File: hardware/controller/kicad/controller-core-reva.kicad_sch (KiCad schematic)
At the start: 198 parts, among them J101 12V_ISOLATED_INPUT / JST XH, J102 STM_SWD / 1x6 2.54mm, J103 ESP_UART / 1x6 2.54mm, J104 UI_LINK / WR-MM 16, J105 JP13 NTC / 2 vías, J106 JP5 FLOW ADAPTER / VCC-GND-OC, J107 JP14 DOOR / contacto seco, J108 JP16 VISUAL V1..V8 / XH-8, J109 JP22 WATER / RED-WHITE-BLACK, J110 USB-C SERVICE / USB 2.0, J111 USB BENCH POWER / OPEN, J112 24V_ACTUATOR_INPUT / JST XH, J113 JP3 VALVE / A2506, J114 POWER MONITOR / MEASURE ONLY, J115 JP8 GRINDER / 320VDC, J116 JP19 HEATER / 1900W 27R5, J117 JP24 PUMP / 230VAC, J118 JP17 MAINS / L-N, J119 JP1 PE TO BOILER, J120 JP9 PE INPUT, J121 24V INTERNAL SELECT / OPEN FO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, K701 G5RL-1A-E-TV8 DC24, Q501 SI2308A, Q701 BSS138LT1G / relay coil, Q703 BTA24-800BWRG / heater, Q704 BTA24-800BWRG / pump, Q705 BSS138LT1G / heater opto LED, Q706 BSS138LT1G / pump opto LED, Q707 BSS138LT1G / grinder opto LED, Q708 BTA24-800BWRG / grinder, U101 STM32G431RBT6, U201 ESP32-S3-WROOM-1U-N8R8, U203 USBLC6-2SC6, U301 AP63203WU-7, U302 TPS22918DBVR, U303 AP63200WU-7 / 24V to 12V, U501 DRV8876PWPR, U502 UCC27517DBVR, U601 TPS3828-33DBVR, U602 SN74LVC2G08DCTR, U603 SN74LVC2G08DCTR, U604 SN74LVC2G08DCTR, U605 SN74LVC1G17DBVR, U606 SN74LVC1G132DBVR, U701 MOC3083 / zero-cross, U702 MOC3083 / zero-cross, U703 MOC3083 / zero-cross, U704 TMCS1133B4AQDVGR / grinder cu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

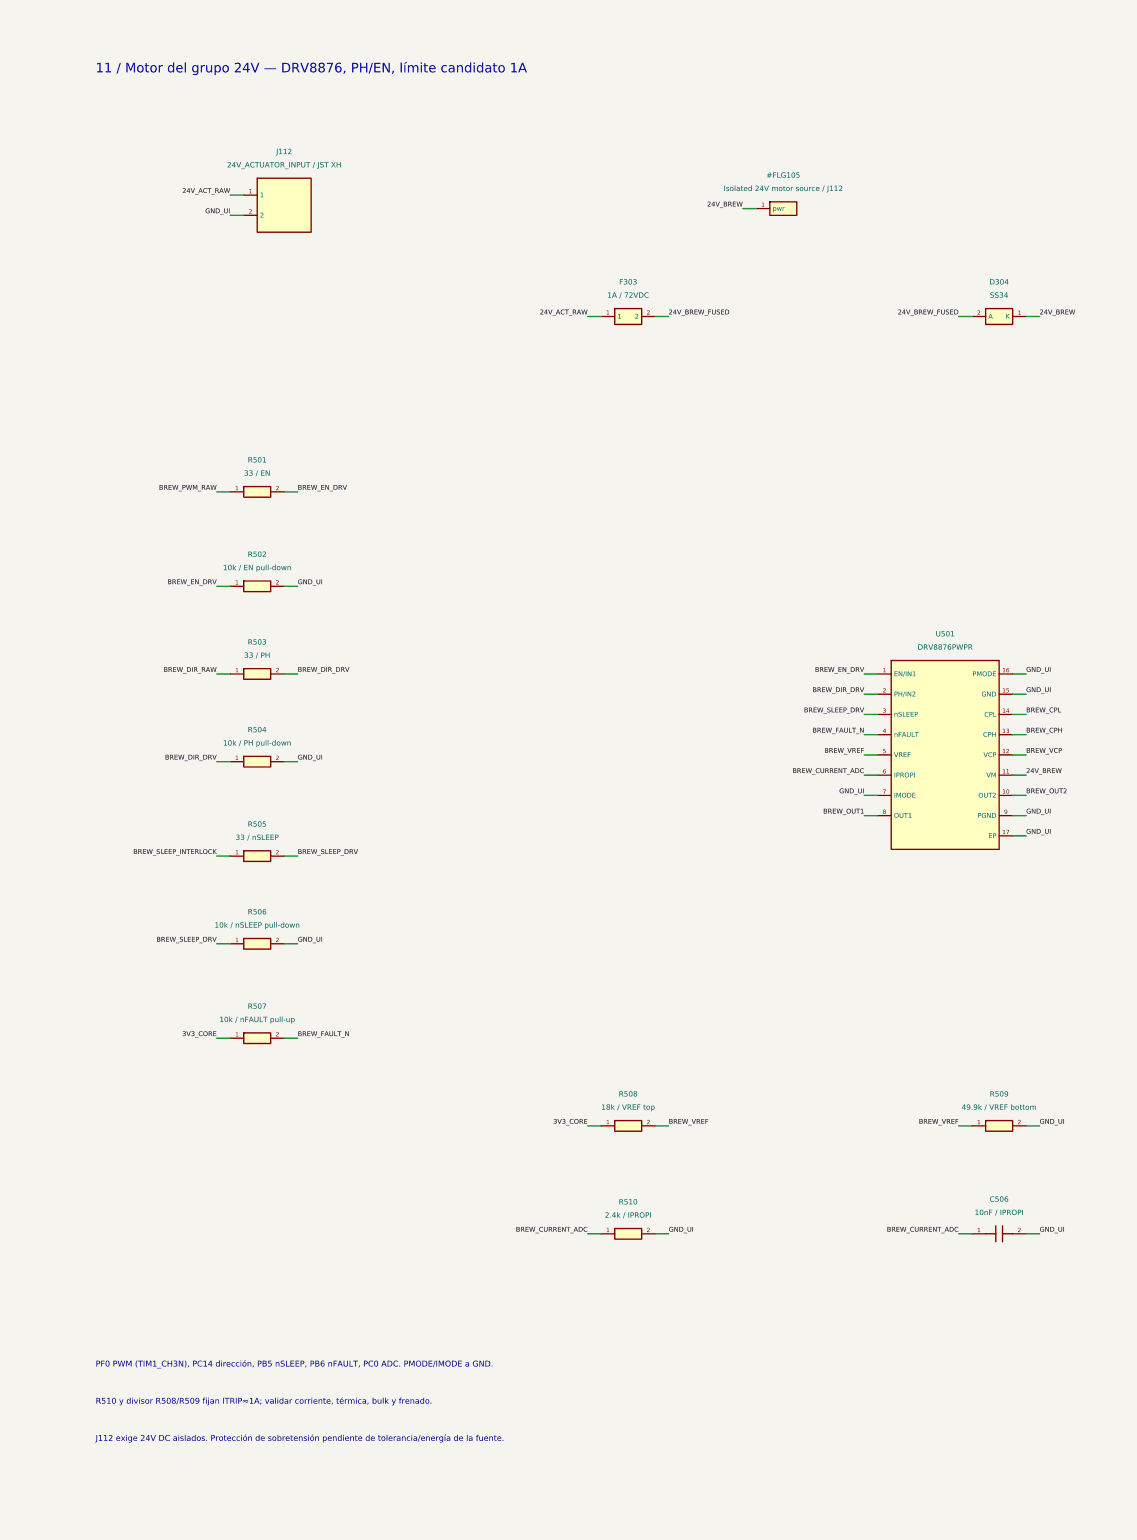
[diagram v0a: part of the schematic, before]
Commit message: Block a reversed bench lead on J112 with its own fuse and Schottky
J112.1 went straight onto 24V_ACT_RAW. With the bench lead reversed,
-24 V reached U303's VIN and EN (AP63200, abs. min -0.3 V) and
forward-biased D701 and Q701's body diode; only the brew and valve
branches had a blocking diode (issue #6).

J112 now reaches the rail through F306 (prosemi 1206TD-2A, C2838912)
and D308 (SS34), like J101 through F305/D307. F306 is 2 A because on
the bench it carries the whole board: the brew motor up to its 1 A
ITRIP, the valve at 0.42 A and the 12 V buck. PS701 still joins through
J121, which stays open whenever J112 is used.

On the PCB both stand in the 24 V lane at x = 112.5 mm under J112; the
lane now ends at D308's cathode, and U303 and C310 take the rail below
the diode and climb back on B.Cu at x = 115.6 mm.

The board model gains a reverse-polarity rule: from every hand-wired
bench input (external_supplies.unkeyed: J101.1, J112.1) it follows
fuses and inductors and fails if a reversed lead reaches anything but
a series diode's anode, a TVS to ground, resistors, unpolarised
capacitors, a relay coil or connectors. On the old netlist it flags
D701.K, U303.EN and U303.VIN. Two mutation tests: J112 back on the rail
and D308 reversed. PS-05 adds the bench reversal test.

ERC 0 on both boards; netlist 200 components / 652 pins; DRC with all
severities 0 violations, 0 unconnected, parity only MH1-MH3; board
model 0 errors, 0 warnings; tests/sim 87/87; CTest 3/3.

Co-Authored-By: Claude Opus 5.5 <noreply@anthropic.com>
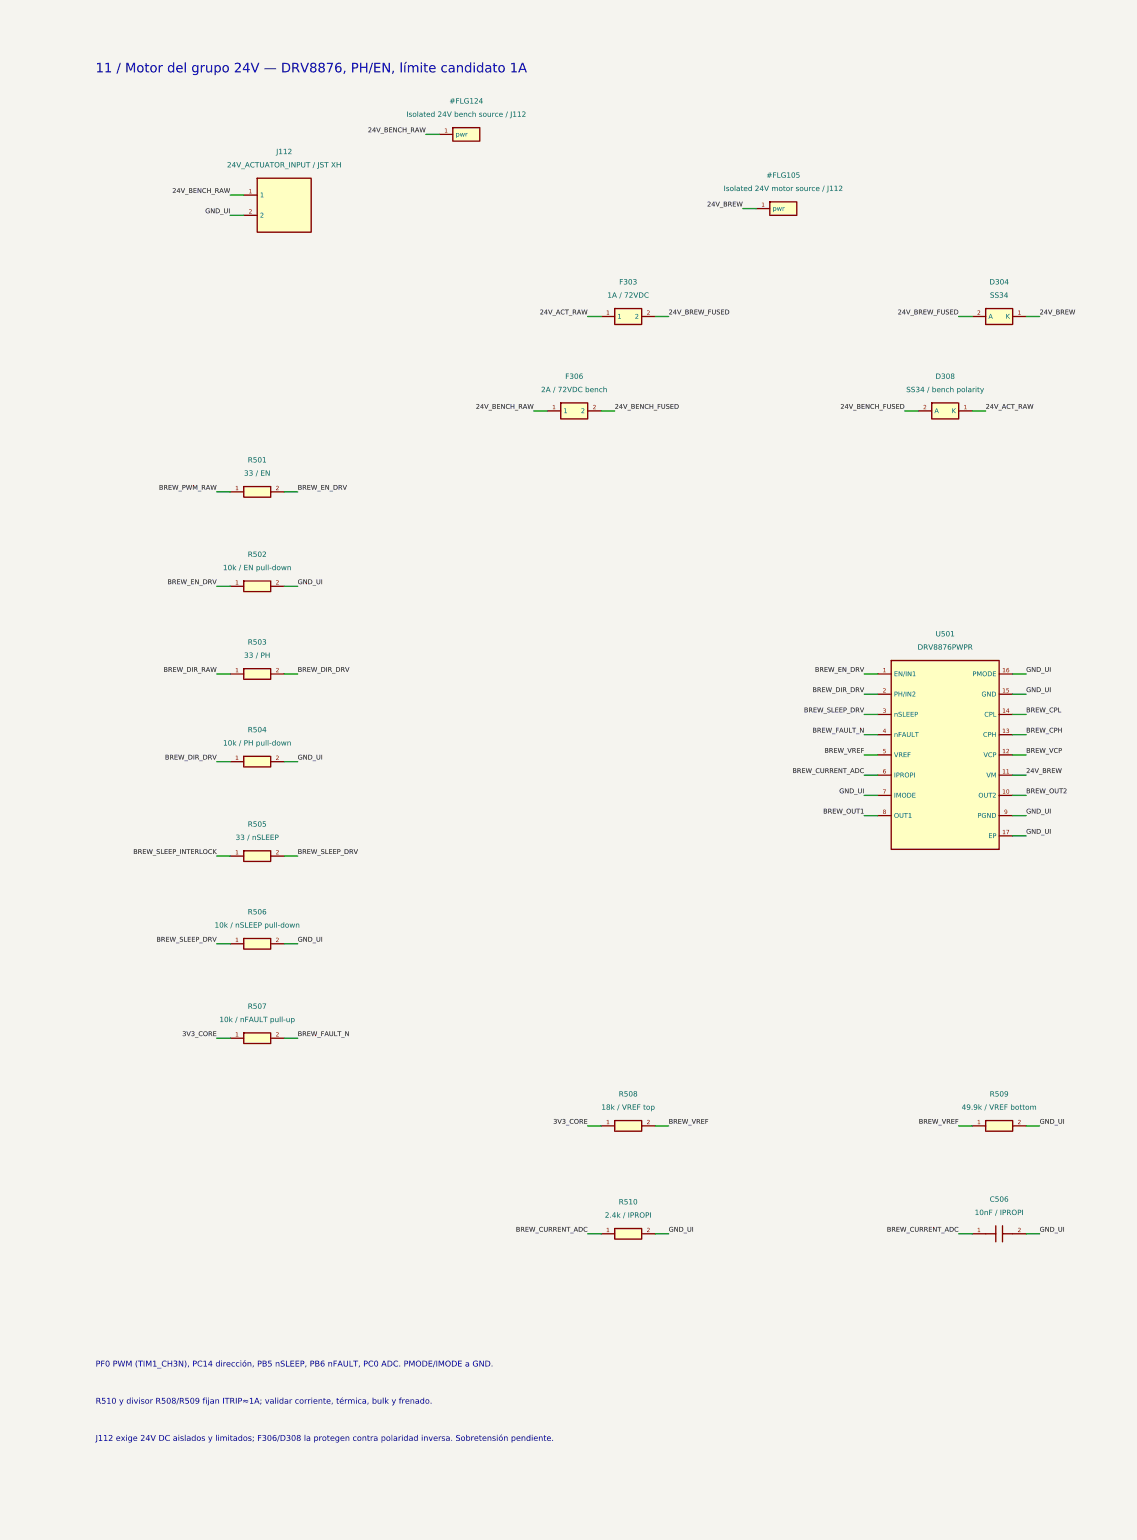
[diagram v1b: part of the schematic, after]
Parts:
- added D308: SS34 / bench polarity, Diode_SMD:D_SMA, symbol OpenSaeco:DIODE
- added F306: 2A / 72VDC bench, Fuse:Fuse_1206_3216Metric, symbol OpenSaeco:FUSE
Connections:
- net 24V_ACT_RAW: now also D308.1 (K); no longer J112.1
- new net 24V_BENCH_FUSED: D308.2 (A), F306.2
- new net 24V_BENCH_RAW: F306.1, J112.1
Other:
- note added: "J112 exige 24V DC aislados y limitados; F306/D308 la protegen contra polaridad inversa. Sobretensión pendiente."
- note removed: "J112 exige 24V DC aislados. Protección de sobretensión pendiente de tolerancia/energía de la fuente."

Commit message: Put a ground between every J114 rail and 10k behind each one
J114 carried GND, 3.3 V, 12 V, 24 V and both ADC nodes on adjacent pins
with nothing in series: a slipped probe put 12 V on 3V3_CORE (2-3),
24 V on 12V_PROTECTED against the SMAJ15A (3-4) or 24 V into PF1 (4-5)
(issue #4).

The header keeps its footprint and place but now reads GND, 3.3 V, GND,
12 V, GND, 24 V, marked "G 3V3 G 12 G 24" on the silkscreen. Each rail
reaches its pin through 10k in 0603 (R723-R725): a slip to ground draws
2.4 mA and 58 mW at 24 V, 0.1 % error on a 10 MOhm meter. The ADC nodes
left the header; they are probed at C701 and C702.

The pads no longer serve as junctions: 12 V joins at a via above the
header and drops between J114.3 and J114.4 to R701 and R724, PF1 drops
between J114.4 and J114.5 to a B.Cu hop, PC1 goes round J114.6 on B.Cu
and the 24 V branch ends at R725. J114 also stops overlapping C603 in
the schematic.

The board model gains a probe-header rule (probe_headers in the
contract): neighbouring pins may not carry two different non-ground
nets, and each rail pin must reach the board only through at least
1 kOhm. On the old pin-out it flags all four adjacent pairs and all six
direct pins. Three mutation tests. The contract follows the rail
telemetry from R701.1/R704.1 instead of J114.5/J114.6.

ERC 0 on both boards; netlist 203 components / 658 pins; DRC with all
severities 0 violations, 0 unconnected, parity only MH1-MH3; board
model 0 errors, 0 warnings; tests/sim 90/90; CTest 3/3.

Co-Authored-By: Claude Opus 5.5 <noreply@anthropic.com>
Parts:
- added R723: 10k / J114 3V3 probe, Resistor_SMD:R_0603_1608Metric, symbol OpenSaeco:R
- added R724: 10k / J114 12V probe, Resistor_SMD:R_0603_1608Metric, symbol OpenSaeco:R
- added R725: 10k / J114 24V probe, Resistor_SMD:R_0603_1608Metric, symbol OpenSaeco:R
- J114: value POWER MONITOR / MEASURE ONLY -> POWER PROBE / MEASURE ONLY
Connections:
- net 12V_PROTECTED: now also R724.1; no longer J114.3
- net 24V_ACT_RAW: now also R725.1; no longer J114.4
- net 3V3_CORE: now also R723.1; no longer J114.2
- net GND_UI: now also J114.3, J114.5
- net RAIL_12V_ADC: no longer J114.5
- net RAIL_24V_ADC: no longer J114.6
- new net PROBE_12V: J114.4, R724.2
- new net PROBE_24V: J114.6, R725.2
- new net PROBE_3V3: J114.2, R723.2
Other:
- note added: "J114: GND, 3V3, GND, 12V, GND, 24V, cada raíl por 10k. Solo medida; ADC en C701/C702."
- note removed: "J114 es de medida; no inyectar alimentación. 12V/24V comparten GND aislada de banco."
- moved on the sheet: J114

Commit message: Put each buck's input capacitors at its VIN and GND pins
U301's bulk input capacitor, C301, was about 30 mm of trace from VIN,
and U303's only one, C310, 8.3 mm away with its ground through two vias
and the plane; Diodes asks for the VIN capacitors as close to the part
as possible (issue #3).

- U301: new C315, 10 uF/50 V X7R 1206 (the C310 part), right behind
  C302, about 5 mm of trace from VIN, with its ground via east of the
  pad. C301 stays as the rail's bulk by D301/D307. At 12 V C315 runs at
  24 % of its rating, against 48 % for the 25 V 0805 C301.
- U303: new C316, 100 nF/50 V, across pins 3 and 4 at 1.7 mm, and C310
  under it at about 4 mm. The 24 V lane enters C310, then C316, then the
  pins; both grounds return to pin 4 on F.Cu, with one via to the plane
  past C310.

tools/check_controller_pcb.py adds the geometric rule the netlist model
cannot express: for U301 and U303, a bulk (>= 4.7 uF) capacitor within
5 mm and a high-frequency one (<= 1 uF) within 3 mm of both VIN and GND,
pin to pad. --self-test moves C315, C316 and C310 in memory and expects
each to fail; on the previous board it flags C301 at 16.5 mm and U303
without a high-frequency capacitor. PS-07 adds the VIN ripple and step
measurement; the effective capacitance under DC bias is still to read.

ERC 0 on both boards; netlist 205 components / 662 pins; DRC with all
severities 0 violations, 0 unconnected, parity only MH1-MH3;
check_controller_pcb --self-test passes; board model 0 errors,
0 warnings; tests/sim 90/90; CTest 3/3.

Co-Authored-By: Claude Opus 5.5 <noreply@anthropic.com>
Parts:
- added C315: 10uF / 50V U301 VIN, Capacitor_SMD:C_1206_3216Metric, symbol OpenSaeco:C
- added C316: 100nF / U303 VIN HF, Capacitor_SMD:C_0603_1608Metric, symbol OpenSaeco:C
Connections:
- net 12V_PROTECTED: now also C315.1
- net 24V_ACT_RAW: now also C316.1
- net GND_UI: now also C315.2, C316.2

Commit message: Current-limit the supplies that leave the board through a harness
J109.1 (JP22) came straight off 3V3_CORE, J106.3 (JP5) off
12V_PROTECTED, and J104.1 (front panel) off a TPS22918 with no current
limit and no thermal shutdown. A short in a harness collapsed the rail
both MCUs run from or could open the one-shot F301, and the reset does
not isolate the front panel since R301 keeps it on (issue #8).

- J104.1: U302 becomes a TPS2553DBVR (C55266). R304 = 49.9k sets
  475-565 mA, under the 1.5 A of the WR-MM contacts and U301's limit,
  with thermal shutdown. R305 = 1k bleeds 3V3_UI as the TPS22918 QOD
  did; the internal soft start replaces C307, which goes. FAULT is open.
- J109.1: U304, a second TPS2553 with R306 = 210k (110-150 mA), C409 on
  its input and C410 at the connector, below J113.
- J106.3: R413, a 390 ohm 0.66 W anti-surge resistor, with C408. Under
  8 mA the Digmesa keeps about 7.9 V of the 3.8 V it needs; a short
  stays at 32 mA and 0.4 W. An NSI45015 constant-current regulator was
  rejected: at 600 C/W on 100 mm2 of copper a short heats it about
  135 C. The pump LED's 12 V branch now ends at R413, not on the JP5 pad.

The board model gains an offboard-supply rule (offboard_supplies in the
contract): each listed pin must come from a switch marked
current_limited in devices.json or only through resistors of at least
100 ohm. Three mutation tests. The simulator's load-switch model takes
both pin namings (VIN/ON/VOUT and IN/EN/OUT). PS-08 adds the short
tests on each output.

ERC 0 on both boards; netlist 212 components / 680 pins; DRC with all
severities 0 violations, 0 unconnected, parity only MH1-MH3;
check_controller_pcb --self-test passes; board model 0 errors,
0 warnings; tests/sim 93/93; CTest 3/3.

Co-Authored-By: Claude Opus 5.5 <noreply@anthropic.com>
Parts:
- removed C307: 1nF / CT, Capacitor_SMD:C_0603_1608Metric, symbol OpenSaeco:C
- added C408: 100nF / FLOW VCC, Capacitor_SMD:C_0603_1608Metric, symbol OpenSaeco:C
- added C409: 100nF / JP22 switch input, Capacitor_SMD:C_0603_1608Metric, symbol OpenSaeco:C
- added C410: 1uF / JP22 VCC, Capacitor_SMD:C_0603_1608Metric, symbol OpenSaeco:C
- added R304: 49.9k / UI ILIM 0.5A, Resistor_SMD:R_0603_1608Metric, symbol OpenSaeco:R
- added R305: 1k / UI discharge, Resistor_SMD:R_0603_1608Metric, symbol OpenSaeco:R
- added R306: 210k / JP22 ILIM 0.13A, Resistor_SMD:R_0603_1608Metric, symbol OpenSaeco:R
- added R413: 390 / FLOW VCC limit, Resistor_SMD:R_1206_3216Metric, symbol OpenSaeco:R
- added U304: TPS2553DBVR / JP22 0.13A limit, Package_TO_SOT_SMD:SOT-23-6, symbol OpenSaeco:TPS2553
- U302: value TPS22918DBVR -> TPS2553DBVR / UI 0.5A limit; symbol OpenSaeco:TPS22918 -> OpenSaeco:TPS2553; lcsc C131941 -> C55266; mpn TPS22918DBVR -> TPS2553DBVR
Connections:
- net 12V_PROTECTED: now also R413.1; no longer J106.3
- net 3V3_CORE: now also C409.1, U304.1 (IN), U304.3 (EN); no longer J109.1
- net 3V3_UI: now also R305.1; no longer U302.5 (QOD)
- net GND_UI: now also C408.2, C409.2, C410.2, R304.2, R305.2, R306.2, U304.2 (GND)
- net UI_RISE: no longer names the net of U302.4 (~{FAULT})
- new net FLOW_VCC: C408.1, J106.3, R413.2
- new net UI_ILIM: R304.1, U302.5 (ILIM)
- new net WATER_ILIM: R306.1, U304.5 (ILIM)
- new net WATER_VCC: C410.1, J109.1, U304.6 (OUT)
- no-connect marks 61 -> 63
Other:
- note added: "08 / Corte y limitación del frontal — TPS2553, 0,5 A"
- note added: "Digmesa 932-9521-B: NPN OC, 3,8–20V. VCC=12V por R413 (390 Ω); pull-up separado a 3V3."
- note added: "ILIM 475-565 mA y apagado térmico; R305 descarga el frontal al apagarlo. FAULT sin conectar."
- note removed: "08 / Corte y descarga del frontal — TPS22918, 2A"
- note removed: "Digmesa 932-9521-B: NPN OC, 3,8–20V. VCC=12V_PROTECTED; pull-up separado a 3V3."
- note removed: "QOD unido a VOUT; CT=1nF limita inrush. Verificar rampa y descarga con el display final."

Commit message: Derate the heater from a heatsink model fed by an air sensor
The design asked about 5 C/W of the triac heatsink, but the reserved
volume (33 x 21 mm, 35 mm tall) only reaches about 8 C/W with a catalogue
profile: the Fischer SK 657 at 37.5 mm, slightly larger, gives 7.75 K/W.
With 8 C/W, Q703 reaches 125 C running the heater continuously above
39 C of air at 253 V (issue #2). The owner chose to keep the volume and
limit the heater by temperature.

- RT701 (Murata NCP18XH103F03RB, C13564), R726 (10k) and C704 (100 nF)
  sit on the SELV edge of the barrier, straight above the heatsink
  column, and reach PB14 (ADC1_IN5, added to sim/reference/mcus.json from
  ST's pin XML). The sensor never touches the profile, which only the
  triacs' insulation separates from mains. Contract signal HEATSINK_AIR:
  0.03-0.07 C/LSB between 40 and 80 C.
- Firmware: osc_heatsink_step() integrates a first-order model of the
  profile (8 C/W, 30 J/K) with each triac's dissipation, and
  osc_heater_cycles_thermal() takes heater cycles away above 105 C of
  estimated junction, down to none at 120 C; a dead RT701 assumes 70 C
  of air. CTest covers a short cold heat-up, an hour with 60 C air and the
  pump on, the dead sensor and the cut-off. Simulated duty after an hour:
  88, 70, 60 and 45 % with 25, 40, 50 and 60 C of air.
- The board model's NTC check no longer divides by zero when a divider
  has no pull-up; mutation test removes R726.
- TH-03 measures the profile, its heat capacity and the RT701
  correlation in a descaling run, with PS701's local air.

ERC 0 on both boards; netlist 215 components / 686 pins; DRC with all
severities 0 violations, 0 unconnected, parity only MH1-MH3;
check_controller_pcb --self-test passes; board model 0 errors,
0 warnings; tests/sim 94/94; CTest 3/3.

Co-Authored-By: Claude Opus 5.5 <noreply@anthropic.com>
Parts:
- added C704: 100nF / heatsink NTC, Capacitor_SMD:C_0603_1608Metric, symbol OpenSaeco:C
- added R726: 10k / heatsink NTC pull-up, Resistor_SMD:R_0603_1608Metric, symbol OpenSaeco:R
- added RT701: 10k B3380 / heatsink air, Resistor_SMD:R_0603_1608Metric, symbol OpenSaeco:NTC
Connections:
- net 3V3_CORE: now also R726.1
- net GND_UI: now also C704.2, RT701.2
- net HS_NTC_ADC: now reaches U101.36 (PB14)
- net HS_NTC_ADC: now also C704.1, R726.2, RT701.1
- no-connect marks 63 -> 62
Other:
- note added: "PB14=ADC1_IN5: aire sobre el disipador (RT701), para limitar el calentador."
